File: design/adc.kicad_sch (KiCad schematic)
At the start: 27 parts, among them J6 JUMPER_DFS/GAIN, U12 TLV431ACDBZR, U13 AD9214

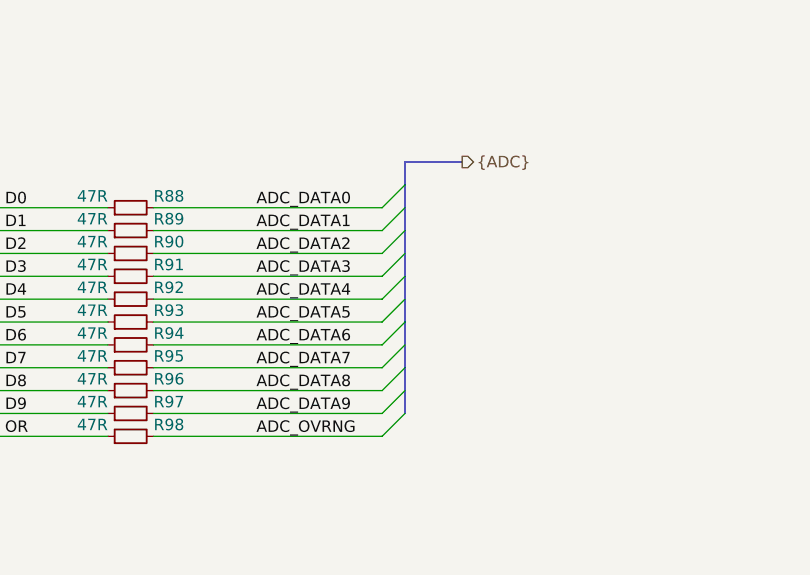
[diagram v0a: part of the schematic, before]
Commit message: Named button reset net
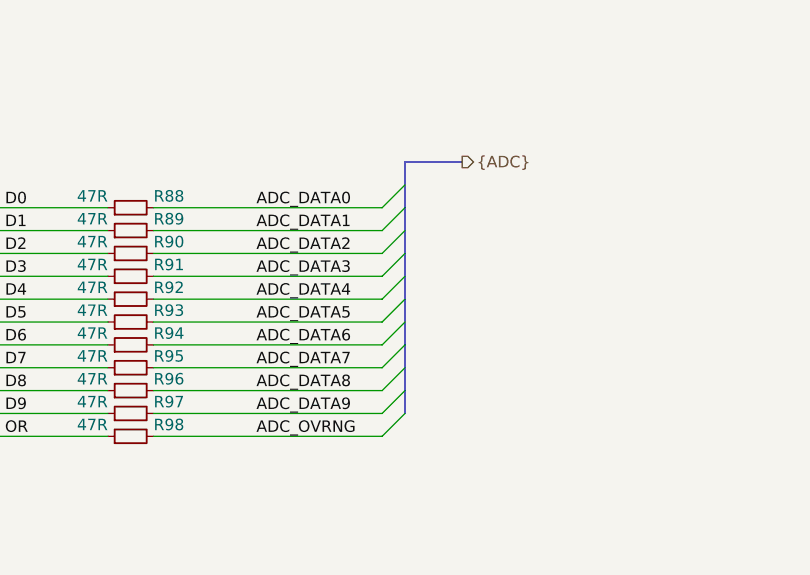
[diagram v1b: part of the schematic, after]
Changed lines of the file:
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@@
 (kicad_sch (version 20200512) (host eeschema "5.99.0-unknown-4efed4b~101~ubuntu18.04.1")
-  (page 7 8)
+  (page 1 8)
   (paper "A4")
   (title_block
@@
   (wire (pts (xy 270.51 53.34) (xy 270.51 54.61)))
   (wire (pts (xy 270.51 62.23) (xy 270.51 63.5)))
-  (bus (pts (xy 214.63 88.9) (xy 214.63 91.44)))
-  (bus (pts (xy 214.63 91.44) (xy 214.63 96.52)))
-  (bus (pts (xy 214.63 96.52) (xy 214.63 101.6)))
-  (bus (pts (xy 214.63 101.6) (xy 214.63 106.68)))
-  (bus (pts (xy 214.63 106.68) (xy 214.63 111.76)))
-  (bus (pts (xy 214.63 111.76) (xy 214.63 116.84)))
+  (bus (pts (xy 214.63 88.9) (xy 214.63 93.98)))
+  (bus (pts (xy 214.63 93.98) (xy 214.63 99.06)))
+  (bus (pts (xy 214.63 99.06) (xy 214.63 104.14)))
+  (bus (pts (xy 214.63 104.14) (xy 214.63 109.22)))
+  (bus (pts (xy 214.63 109.22) (xy 214.63 114.3)))
+  (bus (pts (xy 214.63 114.3) (xy 214.63 116.84)))
   (bus (pts (xy 220.98 88.9) (xy 214.63 88.9)))
   (text "1.24V" (at 40.64 36.83 180)

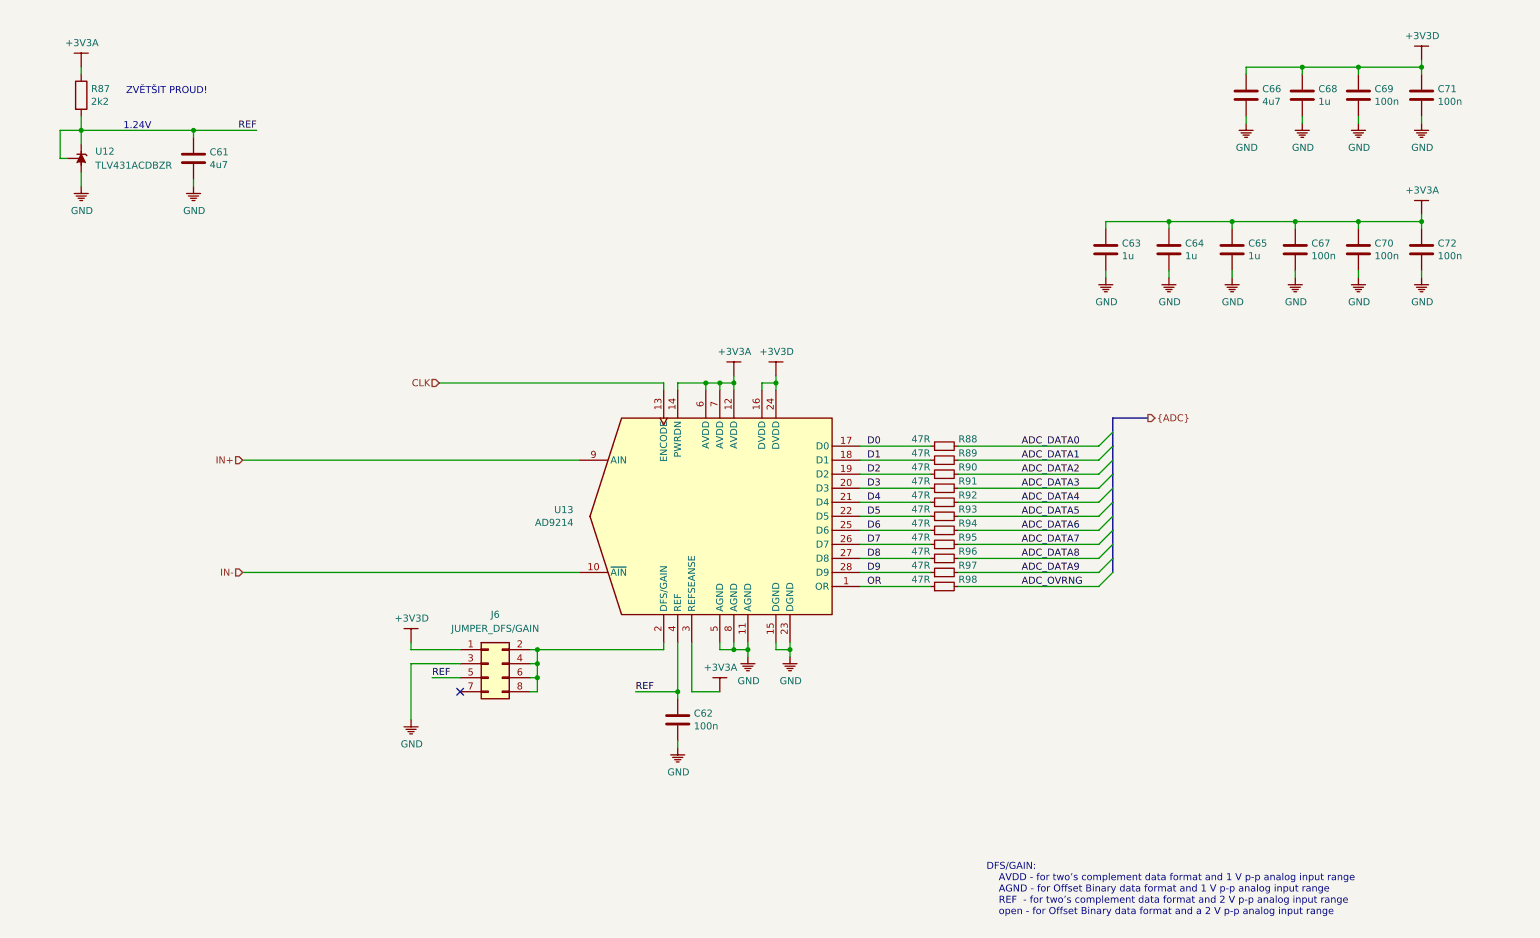
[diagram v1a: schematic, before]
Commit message: Added fiducials
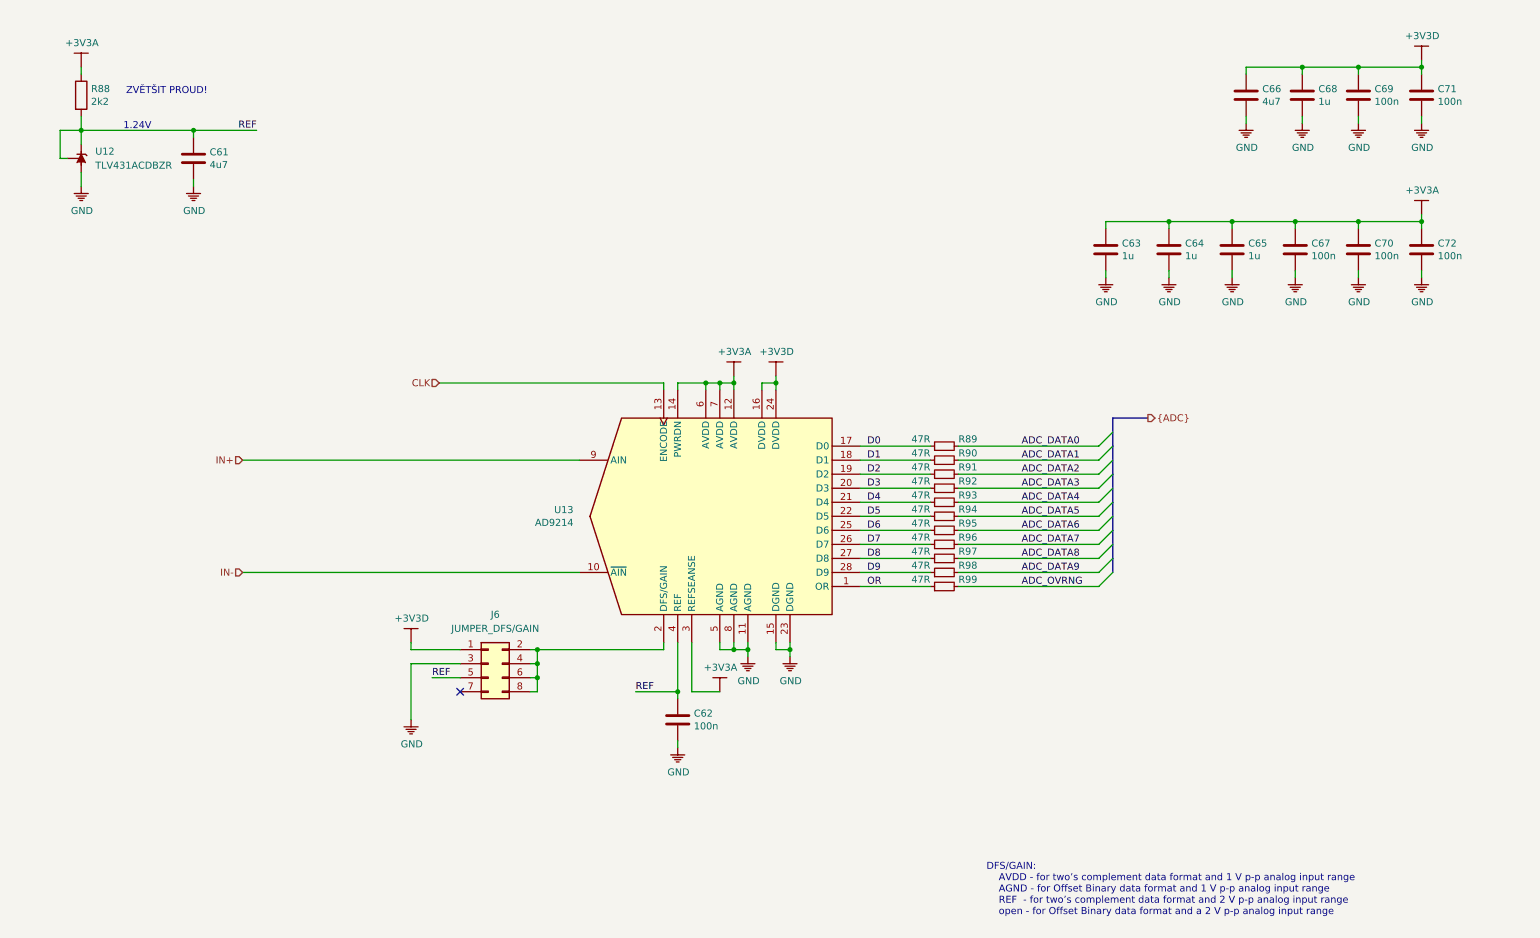
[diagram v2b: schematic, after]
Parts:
- renumbered R87 to R88, R88 to R89, R89 to R90, R90 to R91, R91 to R92, R92 to R93, R93 to R94, R94 to R95, R95 to R96, R96 to R97, R97 to R98, R98 to R99
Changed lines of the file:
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@@
   )
   (symbol (lib_id "KLIB_Power:+3V3A") (at 27.94 25.4 0) (unit 1)
-    (property "Reference" "#PWR0130" (id 0) (at 27.94 33.02 0)
+    (property "Reference" "#PWR0133" (id 0) (at 27.94 33.02 0)
       (effects (font (size 1.27 1.27)) hide)
     )
@@
   )
   (symbol (lib_id "KLIB_Power:GND") (at 27.94 46.99 0) (unit 1)
-    (property "Reference" "#PWR0131" (id 0) (at 27.94 52.07 0)
+    (property "Reference" "#PWR0134" (id 0) (at 27.94 52.07 0)
       (effects (font (size 1.27 1.27)) hide)
     )
@@
   )
   (symbol (lib_id "KLIB_Power:GND") (at 48.26 46.99 0) (unit 1)
-    (property "Reference" "#PWR0132" (id 0) (at 48.26 52.07 0)
+    (property "Reference" "#PWR0135" (id 0) (at 48.26 52.07 0)
       (effects (font (size 1.27 1.27)) hide)
     )
@@
   )
   (symbol (lib_id "KLIB_Power:+3V3D") (at 87.63 129.54 0) (unit 1)
-    (property "Reference" "#PWR0133" (id 0) (at 87.63 137.16 0)
+    (property "Reference" "#PWR0136" (id 0) (at 87.63 137.16 0)
       (effects (font (size 1.27 1.27)) hide)
     )
@@
   )
   (symbol (lib_id "KLIB_Power:GND") (at 87.63 143.51 0) (unit 1)
-    (property "Reference" "#PWR0134" (id 0) (at 87.63 148.59 0)
+    (property "Reference" "#PWR0137" (id 0) (at 87.63 148.59 0)
       (effects (font (size 1.27 1.27)) hide)
     )
@@
   )
   (symbol (lib_id "KLIB_Power:GND") (at 135.89 148.59 0) (unit 1)
-    (property "Reference" "#PWR0135" (id 0) (at 135.89 153.67 0)
+    (property "Reference" "#PWR0138" (id 0) (at 135.89 153.67 0)
       (effects (font (size 1.27 1.27)) hide)
     )
@@
   )
   (symbol (lib_id "KLIB_Power:+3V3A") (at 143.51 138.43 0) (unit 1)
-    (property "Reference" "#PWR0136" (id 0) (at 143.51 146.05 0)
+    (property "Reference" "#PWR0139" (id 0) (at 143.51 146.05 0)
       (effects (font (size 1.27 1.27)) hide)
     )
@@
   )
   (symbol (lib_id "KLIB_Power:+3V3A") (at 146.05 81.28 0) (unit 1)
-    (property "Reference" "#PWR0137" (id 0) (at 146.05 88.9 0)
+    (property "Reference" "#PWR0140" (id 0) (at 146.05 88.9 0)
       (effects (font (size 1.27 1.27)) hide)
     )
@@
   )
   (symbol (lib_id "KLIB_Power:GND") (at 148.59 132.08 0) (unit 1)
-    (property "Reference" "#PWR0138" (id 0) (at 148.59 137.16 0)
+    (property "Reference" "#PWR0141" (id 0) (at 148.59 137.16 0)
       (effects (font (size 1.27 1.27)) hide)
     )
@@
   )
   (symbol (lib_id "KLIB_Power:+3V3D") (at 153.67 81.28 0) (unit 1)
-    (property "Reference" "#PWR0139" (id 0) (at 153.67 88.9 0)
+    (property "Reference" "#PWR0142" (id 0) (at 153.67 88.9 0)
       (effects (font (size 1.27 1.27)) hide)
     )
@@
   )
   (symbol (lib_id "KLIB_Power:GND") (at 156.21 132.08 0) (unit 1)
-    (property "Reference" "#PWR0140" (id 0) (at 156.21 137.16 0)
+    (property "Reference" "#PWR0143" (id 0) (at 156.21 137.16 0)
       (effects (font (size 1.27 1.27)) hide)
     )
@@
   )
   (symbol (lib_id "KLIB_Power:GND") (at 213.36 63.5 0) (unit 1)
-    (property "Reference" "#PWR0141" (id 0) (at 213.36 68.58 0)
+    (property "Reference" "#PWR0144" (id 0) (at 213.36 68.58 0)
       (effects (font (size 1.27 1.27)) hide)
     )
@@
   )
   (symbol (lib_id "KLIB_Power:GND") (at 224.79 63.5 0) (unit 1)
-    (property "Reference" "#PWR0142" (id 0) (at 224.79 68.58 0)
+    (property "Reference" "#PWR0145" (id 0) (at 224.79 68.58 0)
       (effects (font (size 1.27 1.27)) hide)
     )
@@
   )
   (symbol (lib_id "KLIB_Power:GND") (at 236.22 63.5 0) (unit 1)
-    (property "Reference" "#PWR0143" (id 0) (at 236.22 68.58 0)
+    (property "Reference" "#PWR0146" (id 0) (at 236.22 68.58 0)
       (effects (font (size 1.27 1.27)) hide)
     )
@@
   )
   (symbol (lib_id "KLIB_Power:GND") (at 238.76 35.56 0) (unit 1)
-    (property "Reference" "#PWR0144" (id 0) (at 238.76 40.64 0)
+    (property "Reference" "#PWR0147" (id 0) (at 238.76 40.64 0)
       (effects (font (size 1.27 1.27)) hide)
     )
@@
   )
   (symbol (lib_id "KLIB_Power:GND") (at 247.65 63.5 0) (unit 1)
-    (property "Reference" "#PWR0145" (id 0) (at 247.65 68.58 0)
+    (property "Reference" "#PWR0148" (id 0) (at 247.65 68.58 0)
       (effects (font (size 1.27 1.27)) hide)
     )
@@
   )
   (symbol (lib_id "KLIB_Power:GND") (at 248.92 35.56 0) (unit 1)
-    (property "Reference" "#PWR0146" (id 0) (at 248.92 40.64 0)
+    (property "Reference" "#PWR0149" (id 0) (at 248.92 40.64 0)
       (effects (font (size 1.27 1.27)) hide)
     )
@@
   )
   (symbol (lib_id "KLIB_Power:GND") (at 259.08 35.56 0) (unit 1)
-    (property "Reference" "#PWR0147" (id 0) (at 259.08 40.64 0)
+    (property "Reference" "#PWR0150" (id 0) (at 259.08 40.64 0)
       (effects (font (size 1.27 1.27)) hide)
     )
@@
   )
   (symbol (lib_id "KLIB_Power:GND") (at 259.08 63.5 0) (unit 1)
-    (property "Reference" "#PWR0148" (id 0) (at 259.08 68.58 0)
+    (property "Reference" "#PWR0151" (id 0) (at 259.08 68.58 0)
       (effects (font (size 1.27 1.27)) hide)
     )
@@
   )
   (symbol (lib_id "KLIB_Power:+3V3D") (at 270.51 24.13 0) (unit 1)
-    (property "Reference" "#PWR0149" (id 0) (at 270.51 31.75 0)
+    (property "Reference" "#PWR0152" (id 0) (at 270.51 31.75 0)
       (effects (font (size 1.27 1.27)) hide)
     )
@@
   )
   (symbol (lib_id "KLIB_Power:GND") (at 270.51 35.56 0) (unit 1)
-    (property "Reference" "#PWR0150" (id 0) (at 270.51 40.64 0)
+    (property "Reference" "#PWR0153" (id 0) (at 270.51 40.64 0)
       (effects (font (size 1.27 1.27)) hide)
     )
@@
   )
   (symbol (lib_id "KLIB_Power:+3V3A") (at 270.51 52.07 0) (unit 1)
-    (property "Reference" "#PWR0151" (id 0) (at 270.51 59.69 0)
+    (property "Reference" "#PWR0154" (id 0) (at 270.51 59.69 0)
       (effects (font (size 1.27 1.27)) hide)
     )
@@
   )
   (symbol (lib_id "KLIB_Power:GND") (at 270.51 63.5 0) (unit 1)
-    (property "Reference" "#PWR0152" (id 0) (at 270.51 68.58 0)
+    (property "Reference" "#PWR0155" (id 0) (at 270.51 68.58 0)
       (effects (font (size 1.27 1.27)) hide)
     )
@@
   )
   (symbol (lib_id "Device:R_Small") (at 184.15 93.98 90) (unit 1)
-    (property "Reference" "R88" (id 0) (at 186.69 92.71 90)
+    (property "Reference" "R89" (id 0) (at 186.69 92.71 90)
       (effects (font (size 1.27 1.27)) (justify right))
     )
@@
   )
   (symbol (lib_id "Device:R_Small") (at 184.15 96.52 90) (unit 1)
-    (property "Reference" "R89" (id 0) (at 186.69 95.25 90)
+    (property "Reference" "R90" (id 0) (at 186.69 95.25 90)
       (effects (font (size 1.27 1.27)) (justify right))
     )
@@
   )
   (symbol (lib_id "Device:R_Small") (at 184.15 99.06 90) (unit 1)
-    (property "Reference" "R90" (id 0) (at 186.69 97.79 90)
+    (property "Reference" "R91" (id 0) (at 186.69 97.79 90)
       (effects (font (size 1.27 1.27)) (justify right))
     )
@@
   )
   (symbol (lib_id "Device:R_Small") (at 184.15 101.6 90) (unit 1)
-    (property "Reference" "R91" (id 0) (at 186.69 100.33 90)
+    (property "Reference" "R92" (id 0) (at 186.69 100.33 90)
       (effects (font (size 1.27 1.27)) (justify right))
     )
@@
   )
   (symbol (lib_id "Device:R_Small") (at 184.15 104.14 90) (unit 1)
-    (property "Reference" "R92" (id 0) (at 186.69 102.87 90)
+    (property "Reference" "R93" (id 0) (at 186.69 102.87 90)
       (effects (font (size 1.27 1.27)) (justify right))
     )
@@
   )
   (symbol (lib_id "Device:R_Small") (at 184.15 106.68 90) (unit 1)
-    (property "Reference" "R93" (id 0) (at 186.69 105.41 90)
+    (property "Reference" "R94" (id 0) (at 186.69 105.41 90)
       (effects (font (size 1.27 1.27)) (justify right))
     )
@@
   )
   (symbol (lib_id "Device:R_Small") (at 184.15 109.22 90) (unit 1)
-    (property "Reference" "R94" (id 0) (at 186.69 107.95 90)
+    (property "Reference" "R95" (id 0) (at 186.69 107.95 90)
       (effects (font (size 1.27 1.27)) (justify right))
     )
@@
   )
   (symbol (lib_id "Device:R_Small") (at 184.15 111.76 90) (unit 1)
-    (property "Reference" "R95" (id 0) (at 186.69 110.49 90)
+    (property "Reference" "R96" (id 0) (at 186.69 110.49 90)
       (effects (font (size 1.27 1.27)) (justify right))
     )
@@
   )
   (symbol (lib_id "Device:R_Small") (at 184.15 114.3 90) (unit 1)
-    (property "Reference" "R96" (id 0) (at 186.69 113.03 90)
+    (property "Reference" "R97" (id 0) (at 186.69 113.03 90)
       (effects (font (size 1.27 1.27)) (justify right))
     )
@@
   )
   (symbol (lib_id "Device:R_Small") (at 184.15 116.84 90) (unit 1)
-    (property "Reference" "R97" (id 0) (at 186.69 115.57 90)
+    (property "Reference" "R98" (id 0) (at 186.69 115.57 90)
       (effects (font (size 1.27 1.27)) (justify right))
     )
@@
   )
   (symbol (lib_id "Device:R_Small") (at 184.15 119.38 90) (unit 1)
-    (property "Reference" "R98" (id 0) (at 186.69 118.11 90)
+    (property "Reference" "R99" (id 0) (at 186.69 118.11 90)
       (effects (font (size 1.27 1.27)) (justify right))
     )
@@
   )
   (symbol (lib_id "Device:R") (at 27.94 30.48 0) (unit 1)
-    (property "Reference" "R87" (id 0) (at 29.718 29.3116 0)
-      (effects (font (size 1.27 1.27)) (justify left))
-    )
+    (property "Reference" "R88" (id 0) (at 29.718 29.3116 0)
+      (effects (font (size 1.27 1.27)) (justify left))
+    )

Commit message: Updated schematic
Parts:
- R88: value 2k2 -> 1k
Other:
- note added: "- - - -"
- note added: "ADC ANALOG BYPASS"
- note added: "ADC DIGITAL BYPASS"
- note added: "AVDD AGND REF NC"
- note added: "DFS/GAIN:"
- note added: "for two’s complement data format and 1 V_{pp} analog input range for Offset Binary data format and 1 V_{pp} analog input range for two’s complement data format and 2 V_{pp} analog input range for Offset Binary data format and a 2 V_{pp} analog input range"
- note removed: "DFS/GAIN: AVDD - for two’s complement data format and 1 V p-p analog input range AGND - for Offset Binary data format and 1 V p-p analog input range REF - for two’s complement data format and 2 V p-p analog input range open - for Offset Binary data format and a 2 V p-p analog input range"
- note removed: "ZVĚTŠIT PROUD!"
- moved on the sheet: C61, C62, C63, C64, C65, C66, C67, C68, C69, C70, C71, C72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
